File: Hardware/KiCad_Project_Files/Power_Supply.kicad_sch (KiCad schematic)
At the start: 101 parts, among them J2 Conn_01x01, J3 Conn_01x01, J4 Screw_Terminal_01x02, J5 USB_C_Receptacle_USB2.0, Q1 FDN335N, Q2 FDN335N, SW1 UP, SW2 DW, SW3 V_I_SEL, SW4 O_EN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

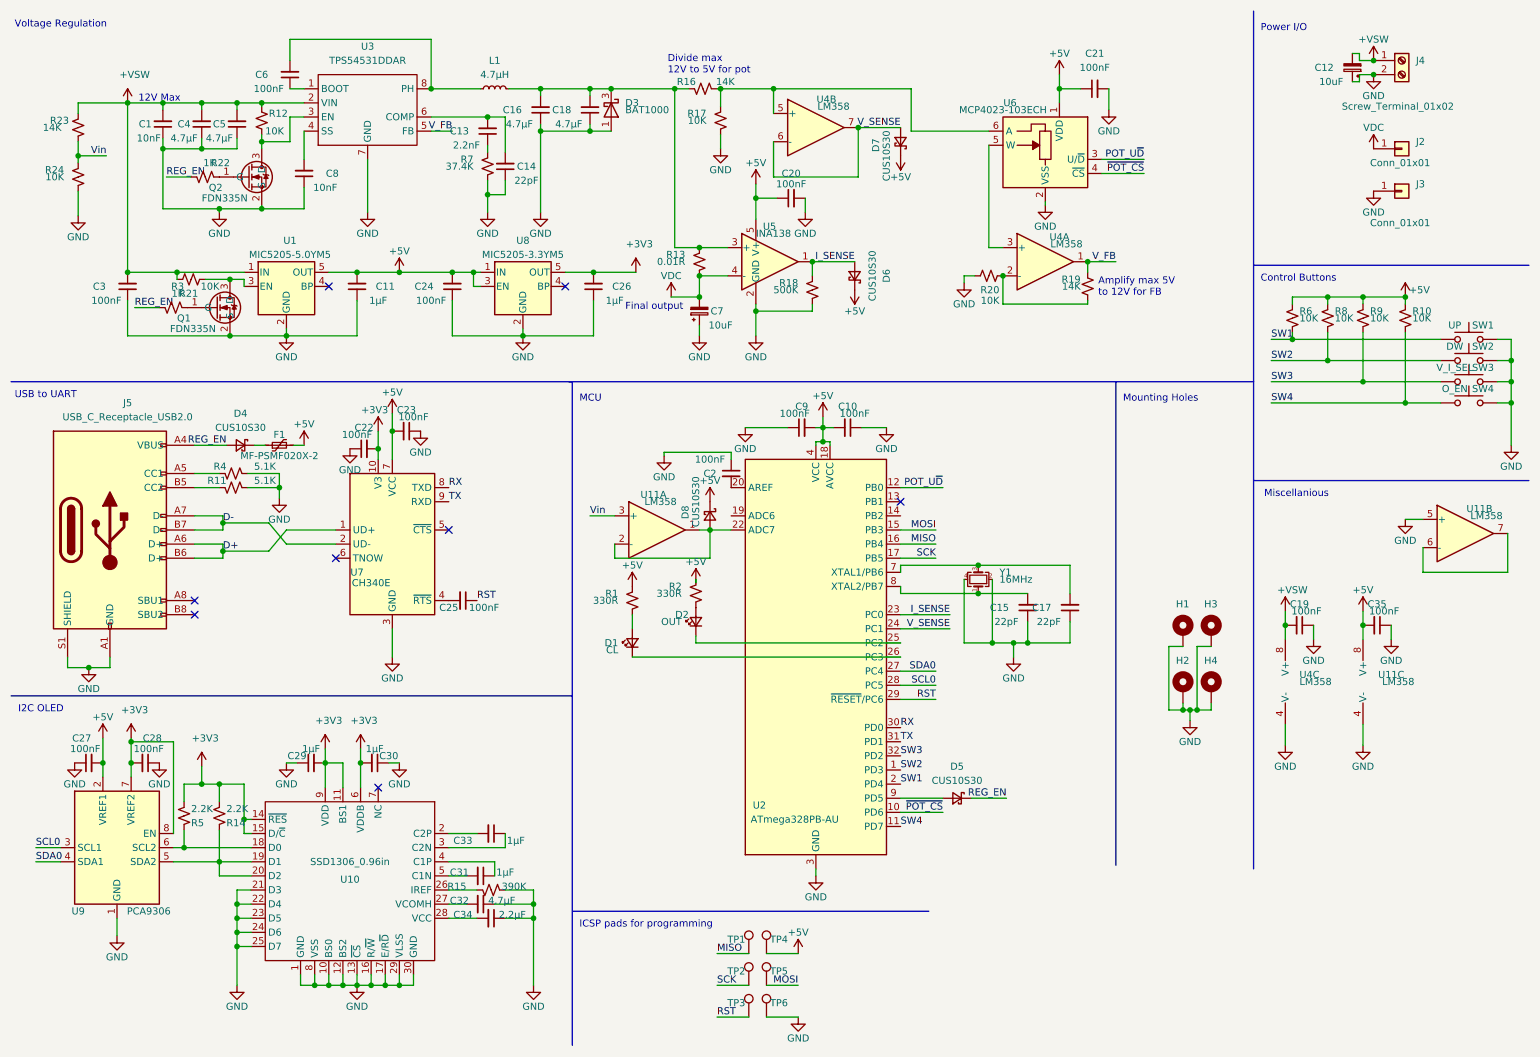
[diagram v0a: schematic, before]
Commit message: added high voltage digi_pot control
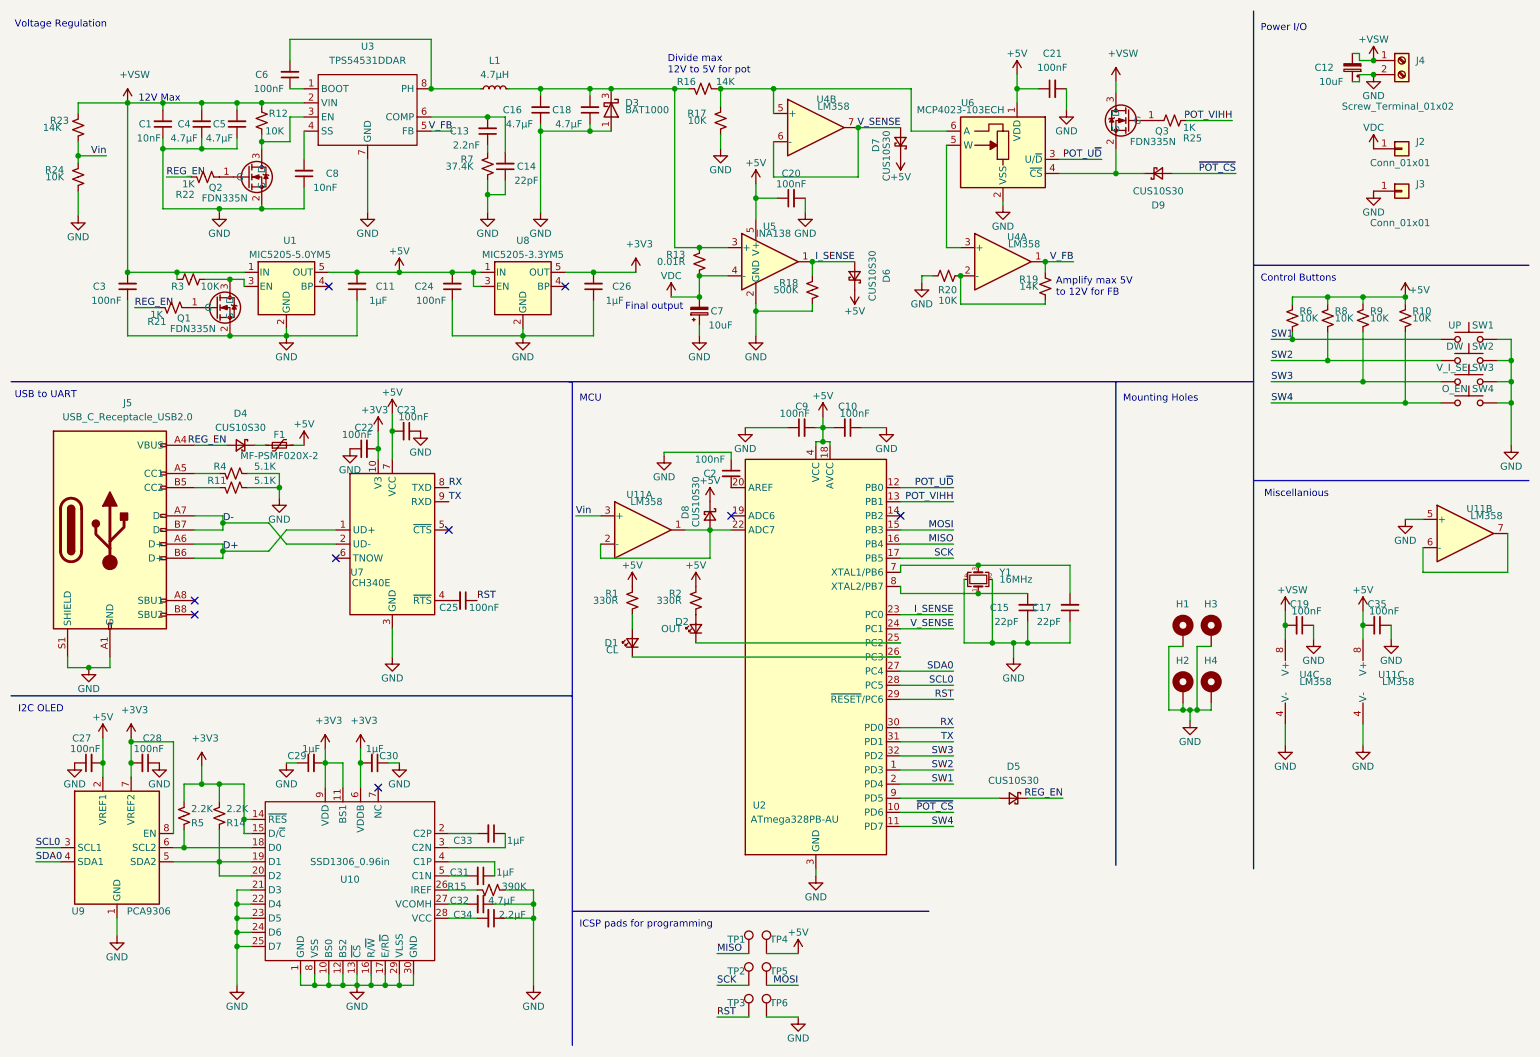
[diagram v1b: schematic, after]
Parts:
- added D9: CUS10S30, Diode_SMD:D_SOD-323, symbol Device:D_Schottky_Small
- added Q3: FDN335N, Package_TO_SOT_SMD:SOT-23, symbol Custom_Transistors:FDN335N
- added R25: 1K, Resistor_SMD:R_0805_2012Metric, symbol Device:R_Small_US
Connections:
- net +VSW: now also Q3.3 (D)
- net ~POT_CS: now also D9.2 (A); no longer U6.4 (~CS)
- net POT_VIHH: now reaches U2.13 (PB1)
- net POT_VIHH: now also R25.2
- new net: Q3.1 (G), R25.1
- new net: D9.1 (K), Q3.2 (S), U6.4 (~CS)
- no-connect marks 8 -> 9
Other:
- moved on the sheet: C21, D2, D5, R19, R2, R20, U11A, U4A, U6
